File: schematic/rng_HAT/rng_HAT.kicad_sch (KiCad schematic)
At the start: 32 parts

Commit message: updating schematic
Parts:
- removed C?: 470uF, Capacitor_SMD:CP_Elec_3x5.3, symbol Device:C_Polarized_Small_US
- removed D?: YEL(WAIT), LED_SMD:LED-APA102-2020, symbol Device:LED
- removed D?: GRN(ON), LED_SMD:LED-APA102-2020, symbol Device:LED
- removed D?: RED(OFF), LED_SMD:LED-APA102-2020, symbol Device:LED
- removed F?: Fan1, Connector_PinHeader_2.54mm:PinHeader_1x01_P2.54mm_Horizontal, symbol Motor:Fan_ALT
- removed F?: Fan2, Connector_PinHeader_2.54mm:PinHeader_1x01_P2.54mm_Horizontal, symbol Motor:Fan_ALT
- removed R? (x2): 220, OptoDevice:R_LDR_4.9x4.2mm_P2.54mm_Vertical, symbol Device:R
- removed R?: 110, OptoDevice:R_LDR_4.9x4.2mm_P2.54mm_Vertical, symbol Device:R
- removed RELAY?: ~, symbol my_parts:wemos_relay
- removed U?: INA3221, Package_DFN_QFN:Texas_RGV0016A_VQFN-16-1EP_4x4mm_P0.65mm_EP2.1x2.1mm, symbol Power_Management:INA3221
- removed U?: BME280, Package_LGA:Bosch_LGA-8_2.5x2.5mm_P0.65mm_ClockwisePinNumbering, symbol Sensor:BME280
- removed U?: BH1750FVI-TR, BH1750FVI-TR:XDCR_BH1750FVI-TR, symbol my_parts:BH1750FVI-TR
- removed U?: TMP36xS, Package_SO:SOIC-8_3.9x4.9mm_P1.27mm, symbol Sensor_Temperature:TMP36xS
- removed U?: SHT30-DIS, Sensor_Humidity:Sensirion_DFN-8-1EP_2.5x2.5mm_P0.5mm_EP1.1x1.7mm, symbol Sensor_Humidity:SHT30-DIS
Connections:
- net at C?.2, D?.1 (K), Q?.1 (E)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: now also U?.10 (PA0)
- net at U?.3 (GPIO2/SDA1): no longer U?.5 (GPIO3/SCL1)
- net at U?. (Vcc): now also U?.11 (PA1)
- net COM: no longer names the net of C?.1, R?.1, R?.1, R?.1, U?. (Vcc), U?.48 (VDD)
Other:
- moved on the sheet: C?, Q?, R?, U?

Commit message: updating shematic
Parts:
- removed U?: ~, symbol my_parts:MQ-6-FF
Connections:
- net STREAM A: now reaches U?.10 (GPIO15/RXD0), U?.42 (PB6)
- net RNG MUX: now reaches U?.11 (GPIO17/GPIO_GEN0)
- net RNG MUX: now also U?.15 (PA5)
- net CS: now reaches U?.12 (GPIO18/GPIO_GEN1)
- net CS: now also U?.25 (PB12)
- net STREAM B: now reaches U?.19 (GPIO10/SPI_MOSI)
- net STREAM B: now also U?.27 (PB14)
- net at U?.21 (GPIO9/SPI_MISO): now also U?.28 (PB15)
- net at U?.23 (GPIO11/SPI_SCLK): now also U?.26 (PB13)
- net I2C_clk: now reaches U?.3 (GPIO2/SDA1)
- net I2C_clk: now also U?.46 (PB9)
- net I2C_dt: now reaches U?.5 (GPIO3/SCL1)
- net I2C_dt: now also U?.45 (PB8)
- net INTRPT?: now reaches U?.43 (PB7), U?.8 (GPIO14/TXD0)
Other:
- note added: "Avalanche"
- moved on the sheet: C?, Q?, R?, U?

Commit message: some stuff
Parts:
- added C?: 100nF, Capacitor_SMD:CP_Elec_3x5.3, symbol Device:C_Polarized_Small_US
- added Q? (x2): 2N3904, Package_TO_SOT_THT:TO-92_Inline, symbol Transistor_BJT:2N3904
- added R? (x2): 4.7k, OptoDevice:R_LDR_4.9x4.2mm_P2.54mm_Vertical, symbol Device:R
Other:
- moved on the sheet: Q?, R?

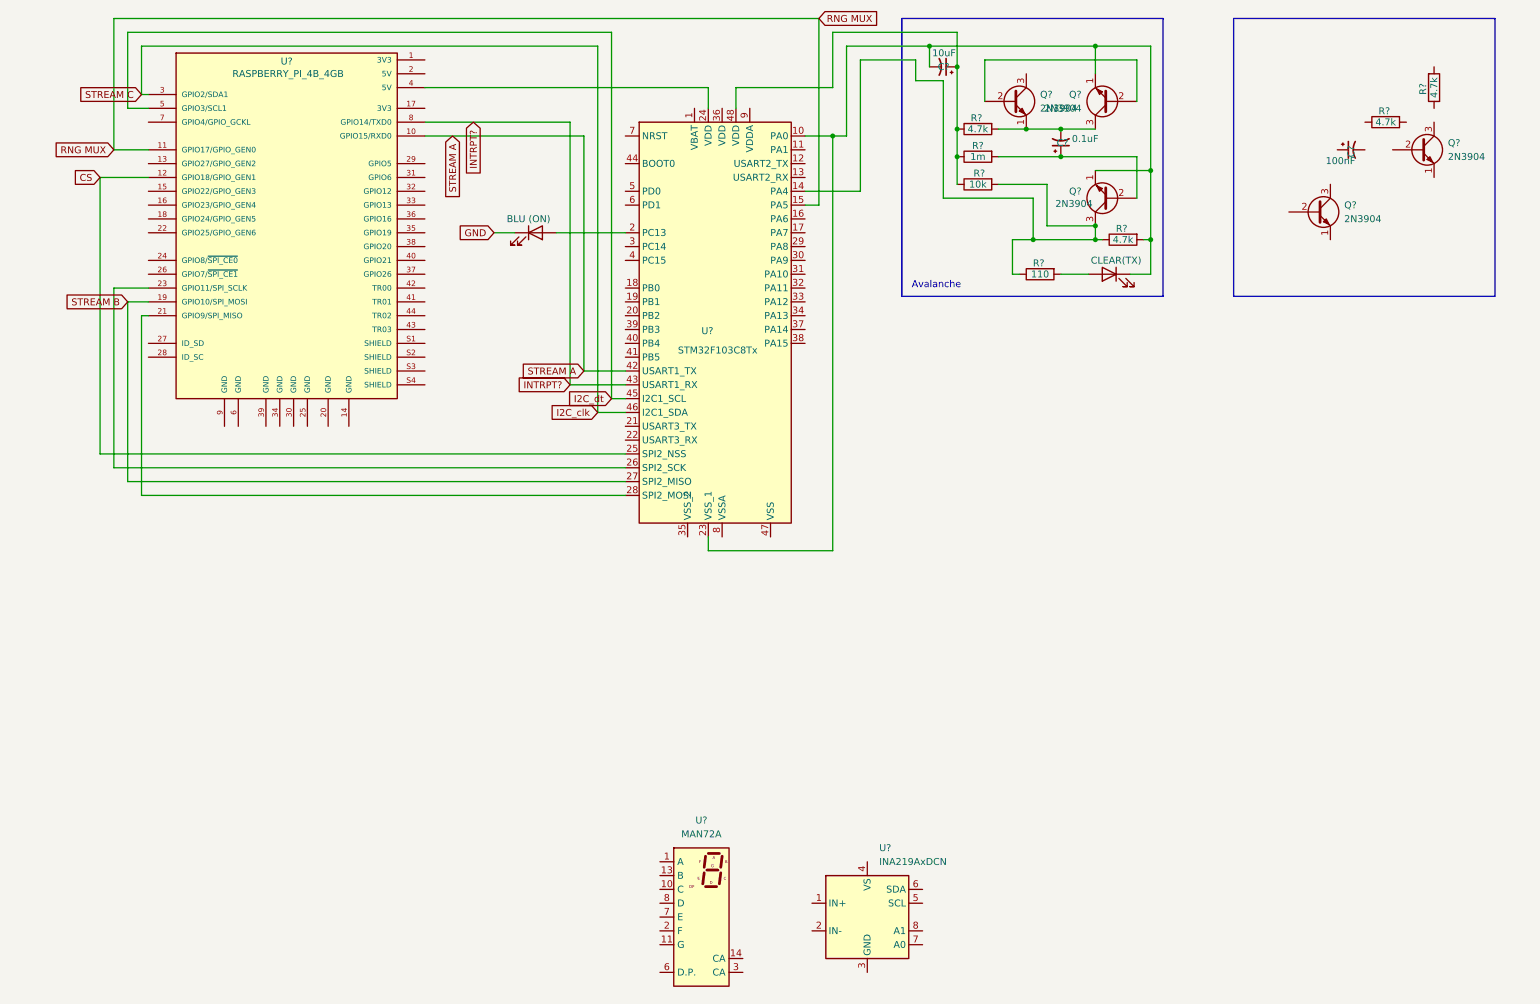
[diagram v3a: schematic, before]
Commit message: adding HAT submodule
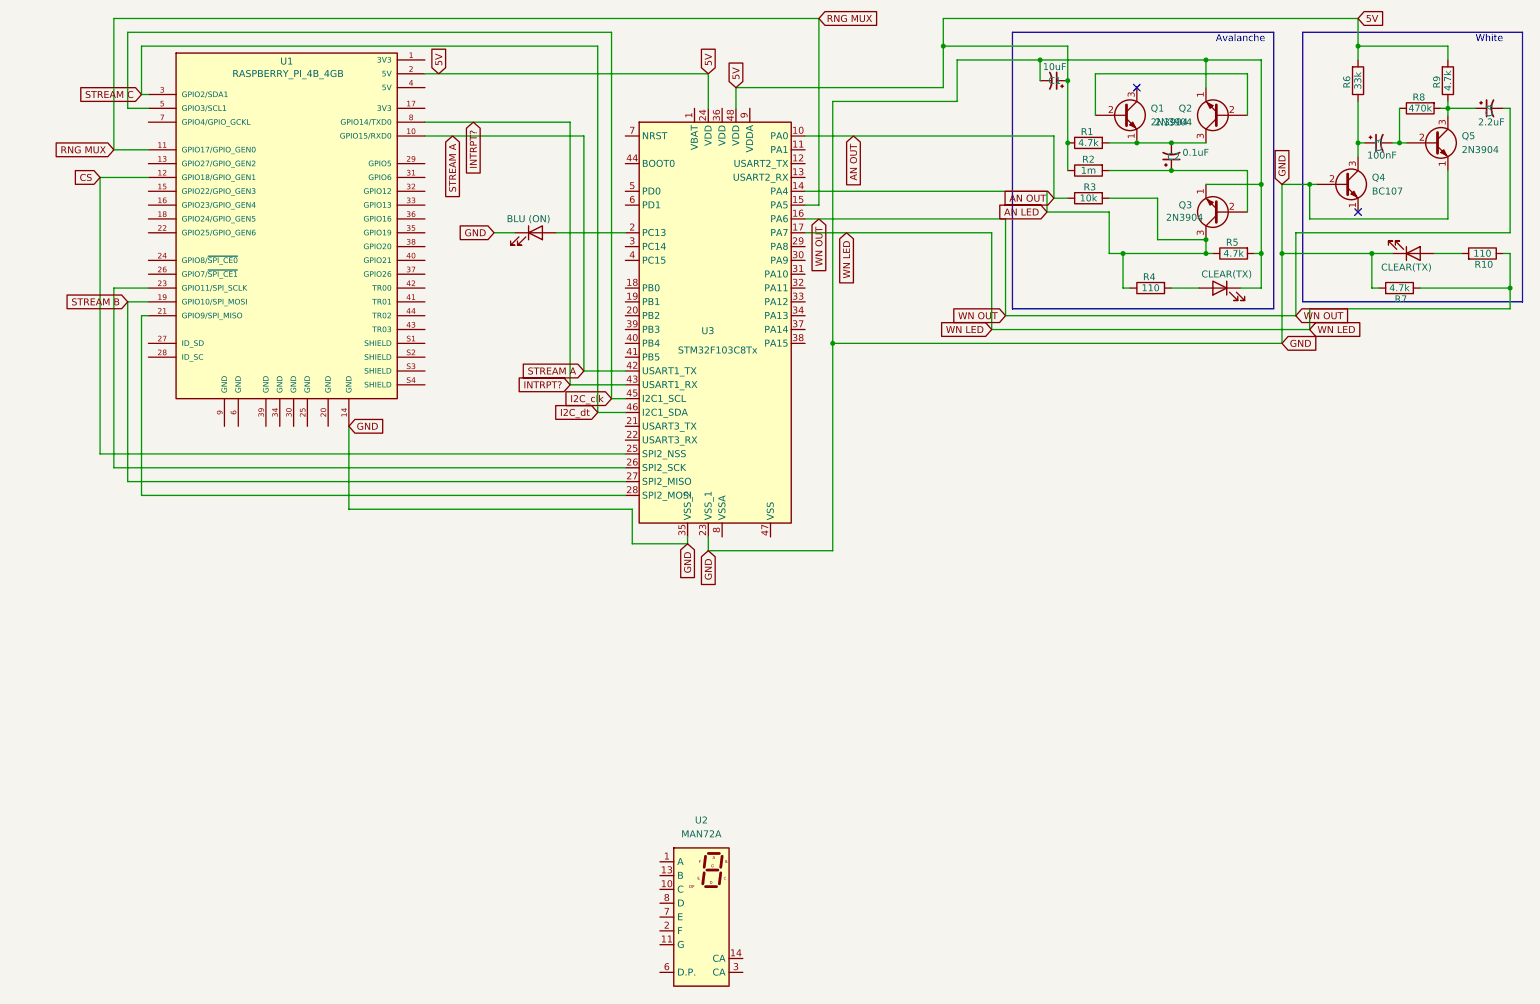
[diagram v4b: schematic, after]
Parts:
- removed Q?: 2N3904, Package_TO_SOT_THT:TO-92_Inline, symbol Transistor_BJT:2N3904
- removed U?: INA219AxDCN, Package_TO_SOT_SMD:SOT-23-8, symbol Sensor_Energy:INA219AxDCN
- added C4: 2.2uF, Capacitor_SMD:CP_Elec_3x5.3, symbol Device:C_Polarized_Small_US
- added D3: CLEAR(TX), LED_SMD:LED-APA102-2020, symbol Device:LED
- added Q4: BC107, Package_TO_SOT_THT:TO-18-3, symbol Transistor_BJT:BC107
- added R10: 110, OptoDevice:R_LDR_4.9x4.2mm_P2.54mm_Vertical, symbol Device:R
- added R6: 33k, OptoDevice:R_LDR_4.9x4.2mm_P2.54mm_Vertical, symbol Device:R
- added R7: 4.7k, OptoDevice:R_LDR_4.9x4.2mm_P2.54mm_Vertical, symbol Device:R
- R8: renamed from R?; value 4.7k -> 470k
- U1: renamed from U?; footprint (none) -> Module:Raspberry_Pi_Zero_Socketed_THT_FaceDown_MountingHoles
- gave numbers to parts that had none: 17
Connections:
- net GND: now also C1.2, D2.1 (K), Q2.1 (E), Q3.1 (E), Q5.1 (E), R5.2, U1.14 (GND), U3.23 (VSS_1), U3.35 (VSS_2), D3.1 (K), Q4.2 (B), R7.2
- net I2C_clk: now also U1.5 (GPIO3/SCL1), U3.45 (PB8); no longer U1.3 (GPIO2/SDA1), U3.46 (PB9)
- net I2C_dt: now also U1.3 (GPIO2/SDA1), U3.46 (PB9); no longer U1.5 (GPIO3/SCL1), U3.45 (PB8)
- net at Q5.2 (B): now also C3.2, R8.1
- net at Q5.3 (C): now also R8.2, R9.1, C4.1
- net AN LED: now reaches Q3.3 (C), R3.2, R4.1, R5.1, U3.14 (PA4)
- net 5V: now reaches U1.2 (5V)
- net 5V: now also C1.1, R1.1, R2.1, R9.2, U3.24 (VDD), U3.48 (VDD), R6.2
- net at U1.4 (5V): no longer U3.24 (VDD)
- net at C3.1: now also Q4.3 (C), R6.1
- net WN OUT: now reaches U3.16 (PA6)
- net WN OUT: now also C4.2
- net WN LED: now reaches U3.17 (PA7)
- net WN LED: now also R10.1, R7.1
- new net: D3.2 (A), R10.2
- new net AN OUT: R3.1, U3.10 (PA0)
- no-connect marks 0 -> 2
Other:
- note added: "White"
- moved on the sheet: C1, C2, C3, Q1, Q2, Q3, Q5, R1, R2, R3, R4, R5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

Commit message: schematic updates
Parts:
- removed U1: RASPBERRY_PI_4B_4GB, Module:Raspberry_Pi_Zero_Socketed_THT_FaceDown_MountingHoles, symbol my_parts:RASPBERRY_PI_4B_4GB
- added J1: RPi_GPIO, symbol RPi_Hat:RPi_GPIO
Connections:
- net 5V: now also J1.2 (5V)
- net CS: now also J1.35 (BCM19_MISO_PCM_FS)
- net GND: now also J1.34 (GND)
- net INTRPT?: now also J1.8 (BCM14_TXD)
- net RNG MUX: now also J1.11 (BCM17)
- net STREAM A: now also J1.10 (BCM15_RXD)
- net STRM SPI(MISO): now reaches U3.28 (PB15)
- net STRM SPI(MISO): now also J1.21 (BCM9_MISO)
- net at U3.26 (PB13): now also J1.23 (BCM11_SCLK)
- net I2C_clk renamed STRM I2C(CLK)
- net STRM I2C(CLK): now also J1.5 (BCM3_SCL)
- net I2C_dt renamed STRM I2C(DT)
- net STRM I2C(DT): now also J1.3 (BCM2_SDA)
- net STREAM B renamed STRM SPI(MOSI)
- net STRM SPI(MOSI): now also J1.19 (BCM10_MOSI)

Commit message: working PCB?
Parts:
- removed U2: MAN72A, Display_7Segment:MAN72A, symbol Display_Character:MAN72A
- D1, D2, D3: footprint LED_SMD:LED-APA102-2020 -> LED_SMD:LED_0201_0603Metric
- J1: footprint (none) -> RPI_Hat:RPI_Hat_B+
- R1, R10, R2, R3, R4, R5, R6, R7, R8, R9: footprint OptoDevice:R_LDR_4.9x4.2mm_P2.54mm_Vertical -> Resistor_SMD:R_0201_0603Metric
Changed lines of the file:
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@@
 			)
 		)
-		(property "Footprint" "OptoDevice:R_LDR_4.9x4.2mm_P2.54mm_Vertical"
+		(property "Footprint" "Resistor_SMD:R_0201_0603Metric"
 			(at 267.462 25.4 90)
 			(effects
@@
 			)
 		)
-		(property "Footprint" "OptoDevice:R_LDR_4.9x4.2mm_P2.54mm_Vertical"
+		(property "Footprint" "Resistor_SMD:R_0201_0603Metric"
 			(at 203.2 45.212 90)
 			(effects
@@
 			)
 		)
-		(property "Footprint" "LED_SMD:LED-APA102-2020"
+		(property "Footprint" "LED_SMD:LED_0201_0603Metric"
 			(at 101.6 53.34 0)
 			(effects
@@
 			)
 		)
-		(property "Footprint" "OptoDevice:R_LDR_4.9x4.2mm_P2.54mm_Vertical"
+		(property "Footprint" "Resistor_SMD:R_0201_0603Metric"
 			(at 275.59 58.928 90)
 			(effects
@@
 			)
 		)
-		(property "Footprint" ""
+		(property "Footprint" "RPI_Hat:RPI_Hat_B+"
 			(at 38.1 24.13 0)
 			(effects
@@
 					(size 1.524 1.524)
 				)
+				(hide yes)
 			)
 		)
@@
 			)
 		)
-		(property "Footprint" "OptoDevice:R_LDR_4.9x4.2mm_P2.54mm_Vertical"
+		(property "Footprint" "Resistor_SMD:R_0201_0603Metric"
 			(at 260.35 65.278 90)
 			(effects
@@
 			)
 		)
-		(property "Footprint" "OptoDevice:R_LDR_4.9x4.2mm_P2.54mm_Vertical"
+		(property "Footprint" "Resistor_SMD:R_0201_0603Metric"
 			(at 264.16 28.702 90)
 			(effects
@@
 			)
 		)
-		(property "Footprint" "OptoDevice:R_LDR_4.9x4.2mm_P2.54mm_Vertical"
+		(property "Footprint" "Resistor_SMD:R_0201_0603Metric"
 			(at 203.2 35.052 90)
 			(effects
@@
 			)
 		)
-		(property "Footprint" "LED_SMD:LED-APA102-2020"
+		(property "Footprint" "LED_SMD:LED_0201_0603Metric"
 			(at 227.33 63.5 0)
 			(effects
@@
 			)
 		)
-		(property "Footprint" "OptoDevice:R_LDR_4.9x4.2mm_P2.54mm_Vertical"
+		(property "Footprint" "Resistor_SMD:R_0201_0603Metric"
 			(at 203.2 40.132 90)
 			(effects
@@
 			)
 		)
-		(property "Footprint" "OptoDevice:R_LDR_4.9x4.2mm_P2.54mm_Vertical"
+		(property "Footprint" "Resistor_SMD:R_0201_0603Metric"
 			(at 214.63 61.722 90)
 			(effects
@@
 			)
 		)
-		(property "Footprint" "LED_SMD:LED-APA102-2020"
+		(property "Footprint" "LED_SMD:LED_0201_0603Metric"
 			(at 262.89 57.15 0)
 			(effects
@@
 				(path "/477dca79-6d5f-49ad-92a9-2ab01bbd6391"
 					(reference "U3")
-					(unit 1)
-				)
-			)
-		)
-	)
-	(symbol
-		(lib_id "Display_Character:MAN72A")
-		(at 132.08 179.07 0)
-		(unit 1)
-		(exclude_from_sim no)
-		(in_bom yes)
-		(on_board yes)
-		(dnp no)
-		(property "Reference" "U2"
-			(at 132.08 161.29 0)
-			(effects
-				(font
-					(size 1.27 1.27)
-				)
-			)
-		)
-		(property "Value" "MAN72A"
-			(at 132.08 163.83 0)
-			(effects
-				(font
-					(size 1.27 1.27)
-				)
-			)
-		)
-		(property "Footprint" "Display_7Segment:MAN72A"
-			(at 119.38 196.85 0)
-			(effects
-				(font
-					(size 1.27 1.27)
-				)
-				(justify left)
-				(hide yes)
-			)
-		)
-		(property "Datasheet" "https://www.digchip.com/datasheets/parts/datasheet/161/MAN3640A-pdf.php"
-			(at 134.112 170.18 0)
-			(effects
-				(font
-					(size 1.27 1.27)
-				)
-				(justify left)
-				(hide yes)
-			)
-		)
-		(property "Description" "Single digit 7 segment red LED common anode left hand decimal"
-			(at 132.08 179.07 0)
-			(effects
-				(font
-					(size 1.27 1.27)
-				)
-				(hide yes)
-			)
-		)
-		(pin "3"
-		)
-		(pin "5"
-		)
-		(pin "4"
-		)
-		(pin "12"
-		)
-		(pin "7"
-		)
-		(pin "11"
-		)
-		(pin "13"
-		)
-		(pin "10"
-		)
-		(pin "14"
-		)
-		(pin "2"
-		)
-		(pin "1"
-		)
-		(pin "8"
-		)
-		(pin "9"
-		)
-		(pin "6"
-		)
-		(instances
-			(project "rng_HAT"
-				(path "/477dca79-6d5f-49ad-92a9-2ab01bbd6391"
-					(reference "U2")
 					(unit 1)
 				)
@@
 			)
 		)
-		(property "Footprint" "OptoDevice:R_LDR_4.9x4.2mm_P2.54mm_Vertical"
+		(property "Footprint" "Resistor_SMD:R_0201_0603Metric"
 			(at 250.952 25.4 90)
 			(effects
@@
 			)
 		)
-		(property "Footprint" "OptoDevice:R_LDR_4.9x4.2mm_P2.54mm_Vertical"
+		(property "Footprint" "Resistor_SMD:R_0201_0603Metric"
 			(at 229.87 55.372 90)
 			(effects
